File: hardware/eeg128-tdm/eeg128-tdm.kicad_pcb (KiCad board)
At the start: 4 copper layers, 190 x 110 mm, 640 parts, among them J1 J1, J10 J10, J11 J11, J2 J2, J3 J3, J4 J4, J5 J5, J6 J6, J7 J7, J8 J8, J9 J9, U1 U1, U10 U10, U11 U11, U12 U12, U13 U13, U14 U14, U15 U15, U16 U16, U17 U17, U18 U18, U19 U19, U2 U2, U20 U20, U21 U21, U22 U22, U23 U23, U24 U24, U25 U25, U26 U26, U27 U27, U3 U3, U4 U4, U5 U5, U6 U6, U7 U7, U8 U8, U9 U9, Y1 Y1

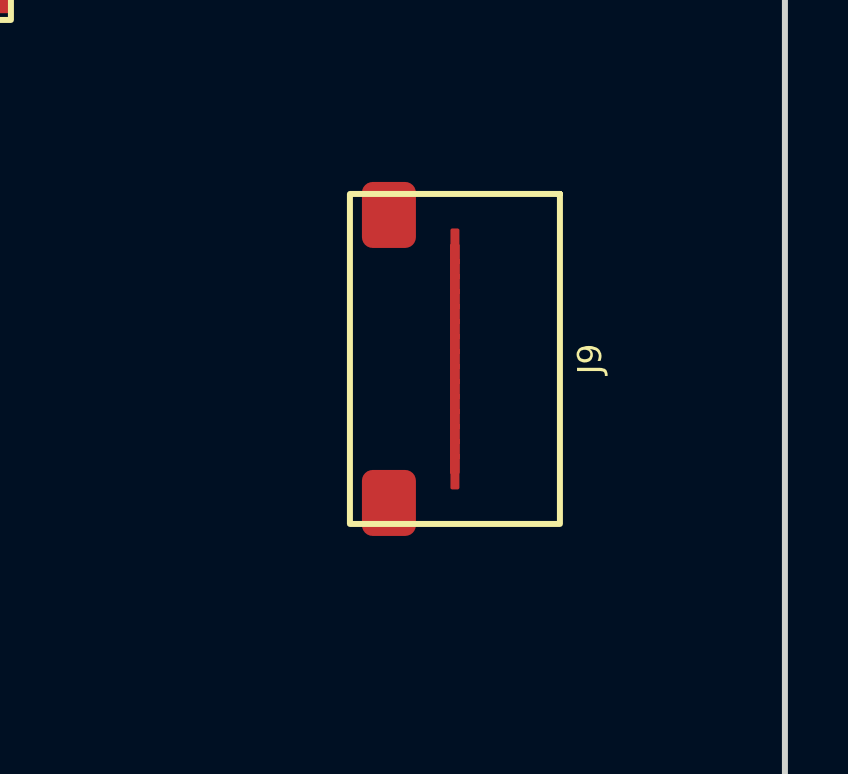
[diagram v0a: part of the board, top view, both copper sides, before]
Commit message: Materialize generated KiCad schematic and release manifest
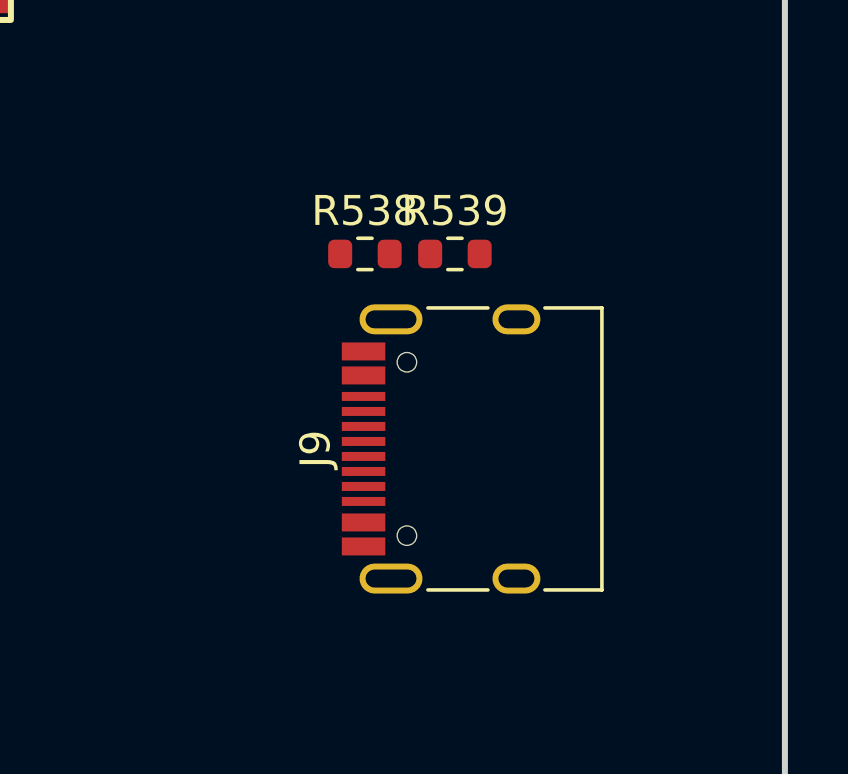
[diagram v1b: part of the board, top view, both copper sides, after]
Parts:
- added R538: 5.1k, R_0603_1608Metric, F.Cu at (181.0, 70.5)
- added R539: 5.1k, R_0603_1608Metric, F.Cu at (184.0, 70.5)
- J9: value J9 -> TYPE-C-31-M-12; footprint NBFM1_A0:J9 -> USB_C_Receptacle_HRO_TYPE-C-31-M-12
- moved J9 3.16 mm to (185.0, 77.0), turned to 90 degrees
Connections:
- C1 pad 1: (no net) -> 3V3A
- C1 pad 2: (no net) -> AGND
- C10 pad 1: (no net) -> 3V3A
- C10 pad 2: (no net) -> AGND
- C11 pad 1: (no net) -> 3V3A
- C11 pad 2: (no net) -> AGND
- C12 pad 1: (no net) -> 3V3A
- C12 pad 2: (no net) -> AGND
- C13 pad 1: (no net) -> 3V3A
- C13 pad 2: (no net) -> AGND
- C14 pad 1: (no net) -> 3V3A
- C14 pad 2: (no net) -> AGND
- C15 pad 1: (no net) -> 3V3A
- C15 pad 2: (no net) -> AGND
- C16 pad 1: (no net) -> 3V3A
- C16 pad 2: (no net) -> AGND
- C17 pad 1: (no net) -> 5V_ISO
- C17 pad 2: (no net) -> AGND
- C18 pad 1: (no net) -> 3V3A
- C18 pad 2: (no net) -> AGND
- C19 pad 1: (no net) -> 5V_ISO
- C19 pad 2: (no net) -> AGND
- C2 pad 1: (no net) -> 3V3A
- C2 pad 2: (no net) -> AGND
- C20 pad 1: (no net) -> 3V3D
- C20 pad 2: (no net) -> AGND
- C21 pad 1: (no net) -> 3V3A
- C21 pad 2: (no net) -> AGND
- C22 pad 1: (no net) -> 3V3A
- C22 pad 2: (no net) -> AGND
- C23 pad 1: (no net) -> 3V3A
- C23 pad 2: (no net) -> AGND
- C24 pad 1: (no net) -> 3V3A
- C24 pad 2: (no net) -> AGND
- C25 pad 1: (no net) -> 3V3A
- C25 pad 2: (no net) -> AGND
- C26 pad 1: (no net) -> 3V3A
- C26 pad 2: (no net) -> AGND
- C27 pad 1: (no net) -> 3V3A
- C27 pad 2: (no net) -> AGND
- C28 pad 1: (no net) -> 3V3A
- C28 pad 2: (no net) -> AGND
- C29 pad 1: (no net) -> 3V3A
- C29 pad 2: (no net) -> AGND
- C3 pad 1: (no net) -> 3V3A
- C3 pad 2: (no net) -> AGND
- C30 pad 1: (no net) -> 3V3A
- C30 pad 2: (no net) -> AGND
- C31 pad 1: (no net) -> 3V3A
- C31 pad 2: (no net) -> AGND
- C32 pad 1: (no net) -> 3V3A
- C32 pad 2: (no net) -> AGND
- C33 pad 1: (no net) -> 3V3A
- C33 pad 2: (no net) -> AGND
- C34 pad 1: (no net) -> 3V3A
- C34 pad 2: (no net) -> AGND
- C35 pad 1: (no net) -> 3V3A
- C35 pad 2: (no net) -> AGND
- C36 pad 1: (no net) -> 3V3A
- C36 pad 2: (no net) -> AGND
- C37 pad 1: (no net) -> 3V3A
- C37 pad 2: (no net) -> AGND
- C38 pad 1: (no net) -> 3V3A
- C38 pad 2: (no net) -> AGND
- C39 pad 1: (no net) -> 3V3A
- C39 pad 2: (no net) -> AGND
- C4 pad 1: (no net) -> 3V3A
- C4 pad 2: (no net) -> AGND
- C40 pad 1: (no net) -> 3V3A
- C40 pad 2: (no net) -> AGND
- C41 pad 1: (no net) -> 3V3A
- C41 pad 2: (no net) -> AGND
- C42 pad 1: (no net) -> 3V3D
- C42 pad 2: (no net) -> AGND
- C43 pad 1: (no net) -> ADC_REFIN
- C43 pad 2: (no net) -> AGND
- C44 pad 1: (no net) -> 3V3D
- C44 pad 2: (no net) -> AGND
- C45 pad 1: (no net) -> 3V3D
- C45 pad 2: (no net) -> AGND
- C46 pad 1: (no net) -> 3V3D
- C46 pad 2: (no net) -> AGND
- C47 pad 1: (no net) -> 3V3D
- C47 pad 2: (no net) -> AGND
- C48 pad 1: (no net) -> 3V3D
- C48 pad 2: (no net) -> AGND
- C49 pad 1: (no net) -> 3V3D
- C49 pad 2: (no net) -> AGND
- C5 pad 1: (no net) -> 3V3A
- C5 pad 2: (no net) -> AGND
- C50 pad 1: (no net) -> VREG_1V1
- C50 pad 2: (no net) -> AGND
- C51 pad 1: (no net) -> VREG_1V1
- C51 pad 2: (no net) -> AGND
- C52 pad 1: (no net) -> VREG_1V1
- C52 pad 2: (no net) -> AGND
- C53 pad 1: (no net) -> 3V3D
- C53 pad 2: (no net) -> AGND
- C54 pad 1: (no net) -> 3V3D
- C54 pad 2: (no net) -> AGND
- C55 pad 1: (no net) -> 3V3D
- C55 pad 2: (no net) -> AGND
- C56 pad 1: (no net) -> 3V3D
- C56 pad 2: (no net) -> AGND
- C57 pad 1: (no net) -> 3V3D
- C57 pad 2: (no net) -> AGND
- C58 pad 1: (no net) -> 3V3D
- C58 pad 2: (no net) -> AGND
- C59 pad 1: (no net) -> 3V3D
- C59 pad 2: (no net) -> AGND
- C6 pad 1: (no net) -> 3V3A
- C6 pad 2: (no net) -> AGND
- C60 pad 1: (no net) -> 3V3D
- C60 pad 2: (no net) -> AGND
- C61 pad 2: DGND -> AGND
- C63 pad 2: DGND -> AGND
- C64 pad 2: DGND -> AGND
- C7 pad 1: (no net) -> 3V3A
- C7 pad 2: (no net) -> AGND
- C8 pad 1: (no net) -> 3V3A
- C8 pad 2: (no net) -> AGND
- C9 pad 1: (no net) -> 3V3A
- C9 pad 2: (no net) -> AGND
- J11 pad 2: ISO_GND -> AGND
- R529 pad 1: VCM_DIV_HI -> 3V3A
- U21 pad 25: DGND -> AGND
- U23 pad 57: DGND -> AGND
- U24 pad 1: (no net) -> 5V_ISO
- U24 pad 2: (no net) -> AGND
- U24 pad 3: (no net) -> 5V_ISO
- U24 pad 5: (no net) -> 3V3A
- U25 pad 1: (no net) -> 5V_ISO
- U25 pad 2: (no net) -> AGND
- U25 pad 3: (no net) -> 5V_ISO
- U25 pad 5: (no net) -> 3V3D
- U26 pad 4: DGND -> AGND
- U27 pad 1: (no net) -> 3V3D
- U27 pad 2: DGND -> AGND
- Y1 pad 2: (no net) -> AGND
- Y1 pad 4: (no net) -> AGND

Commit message: Materialize generated KiCad schematic and release manifest
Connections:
- U23 pad 19: (no net) -> AGND
- U23 pad 51: QSPI_SD0 -> QSPI_SD3
- U23 pad 53: QSPI_SD3 -> QSPI_SD0
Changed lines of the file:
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@@
 			(layers "F.Cu" "F.Paste" "F.Mask")
 			(roundrect_rratio 0.2)
+			(net 29 "AGND")
 		)
 		(pad "20" smd roundrect
@@
 			(layers "F.Cu" "F.Paste" "F.Mask")
 			(roundrect_rratio 0.2)
-			(net 588 "QSPI_SD0")
+			(net 591 "QSPI_SD3")
 		)
 		(pad "52" smd roundrect
@@
 			(layers "F.Cu" "F.Paste" "F.Mask")
 			(roundrect_rratio 0.2)
-			(net 591 "QSPI_SD3")
+			(net 588 "QSPI_SD0")
 		)
 		(pad "54" smd roundrect

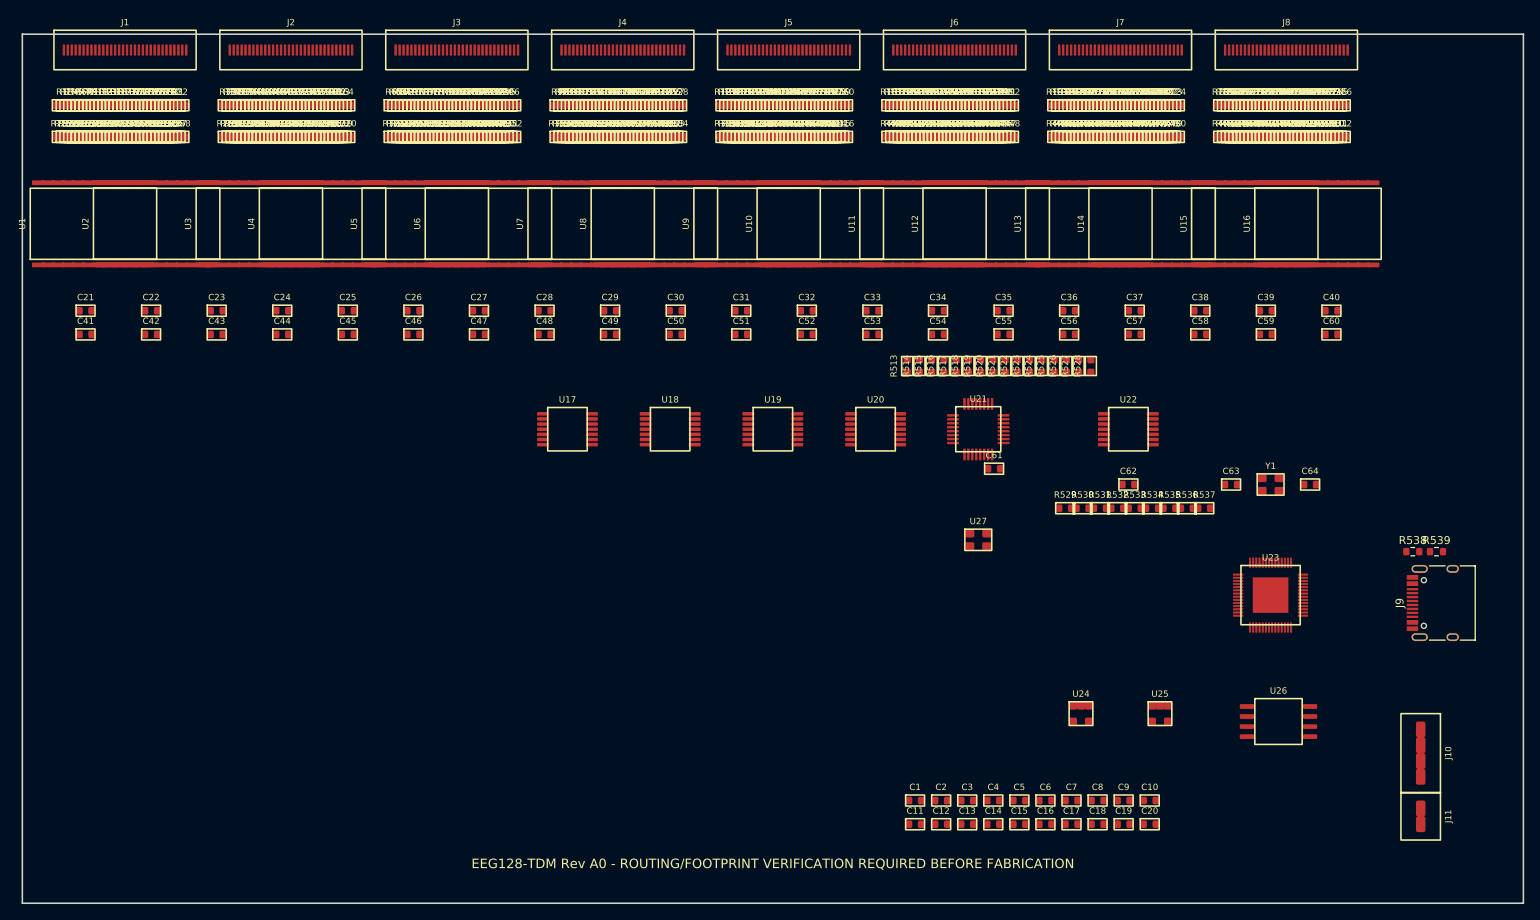
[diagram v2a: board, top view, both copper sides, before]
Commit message: Materialize generated KiCad schematic and release manifest
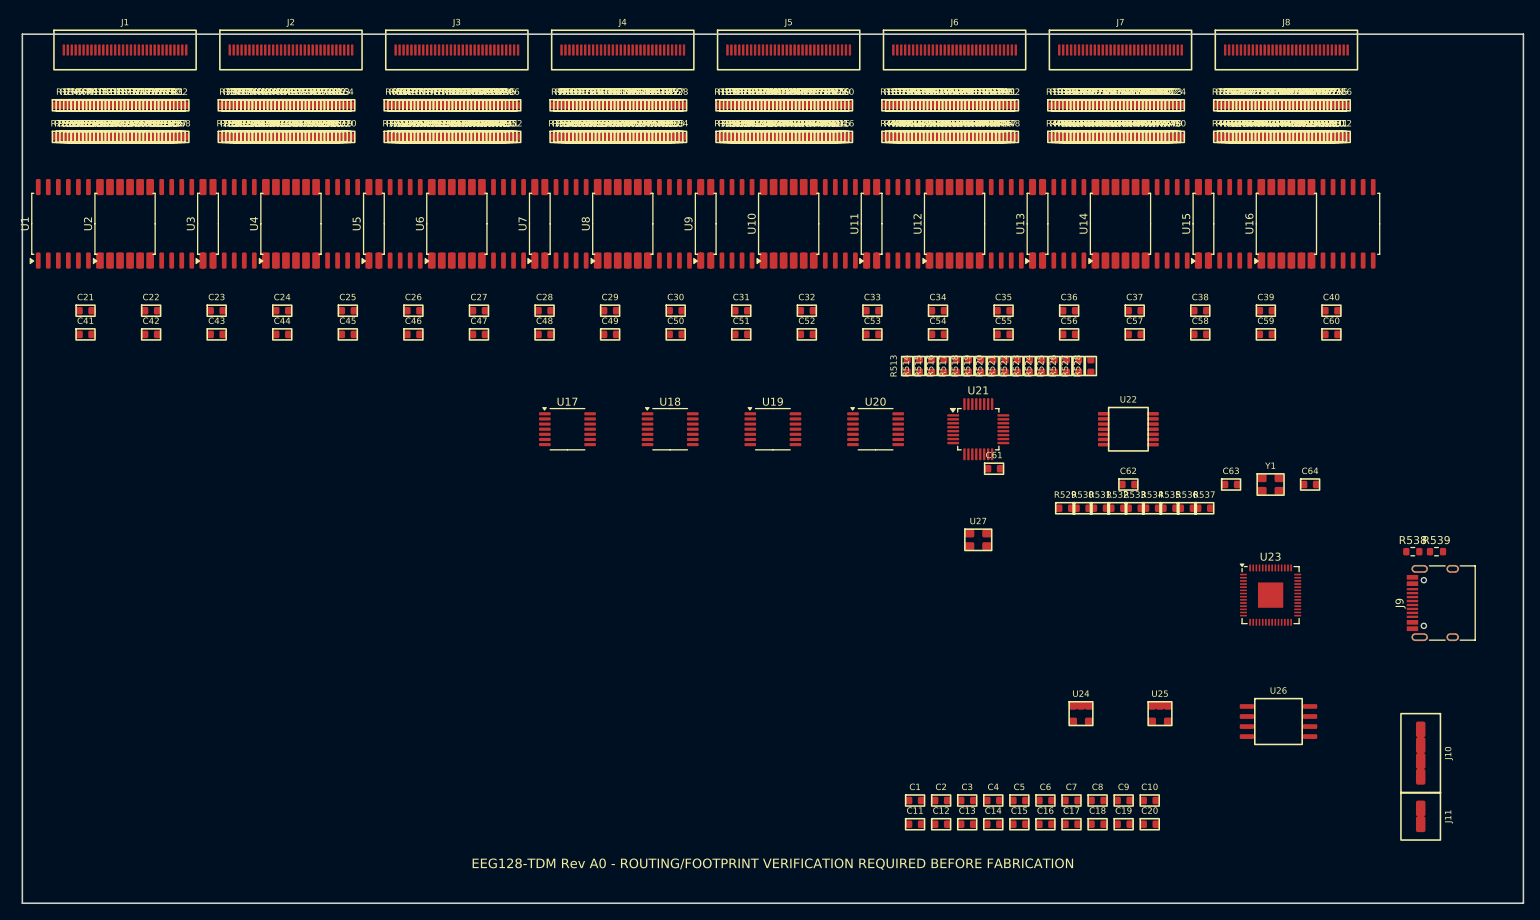
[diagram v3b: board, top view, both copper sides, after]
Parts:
- U1: footprint NBFM1_A0:U1 -> SOIC-24W_7.5x15.4mm_P1.27mm
- U10: footprint NBFM1_A0:U10 -> SOIC-24W_7.5x15.4mm_P1.27mm
- U11: footprint NBFM1_A0:U11 -> SOIC-24W_7.5x15.4mm_P1.27mm
- U12: footprint NBFM1_A0:U12 -> SOIC-24W_7.5x15.4mm_P1.27mm
- U13: footprint NBFM1_A0:U13 -> SOIC-24W_7.5x15.4mm_P1.27mm
- U14: footprint NBFM1_A0:U14 -> SOIC-24W_7.5x15.4mm_P1.27mm
- U15: footprint NBFM1_A0:U15 -> SOIC-24W_7.5x15.4mm_P1.27mm
- U16: footprint NBFM1_A0:U16 -> SOIC-24W_7.5x15.4mm_P1.27mm
- U17: footprint NBFM1_A0:U17 -> TSSOP-14_4.4x5mm_P0.65mm
- U18: footprint NBFM1_A0:U18 -> TSSOP-14_4.4x5mm_P0.65mm
- U19: footprint NBFM1_A0:U19 -> TSSOP-14_4.4x5mm_P0.65mm
- U2: footprint NBFM1_A0:U2 -> SOIC-24W_7.5x15.4mm_P1.27mm
- U20: footprint NBFM1_A0:U20 -> TSSOP-14_4.4x5mm_P0.65mm
- U21: footprint NBFM1_A0:U21 -> LQFP-32_5x5mm_P0.5mm
- U23: footprint NBFM1_A0:U23 -> QFN-56-1EP_7x7mm_P0.4mm_EP3.2x3.2mm
- U3: footprint NBFM1_A0:U3 -> SOIC-24W_7.5x15.4mm_P1.27mm
- U4: footprint NBFM1_A0:U4 -> SOIC-24W_7.5x15.4mm_P1.27mm
- U5: footprint NBFM1_A0:U5 -> SOIC-24W_7.5x15.4mm_P1.27mm
- U6: footprint NBFM1_A0:U6 -> SOIC-24W_7.5x15.4mm_P1.27mm
- U7: footprint NBFM1_A0:U7 -> SOIC-24W_7.5x15.4mm_P1.27mm
- U8: footprint NBFM1_A0:U8 -> SOIC-24W_7.5x15.4mm_P1.27mm
- U9: footprint NBFM1_A0:U9 -> SOIC-24W_7.5x15.4mm_P1.27mm
